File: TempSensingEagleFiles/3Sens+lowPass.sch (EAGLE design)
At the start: 21 parts, among them U1 MLX90614_, U2 MLX90614_, U3 MLX90614_

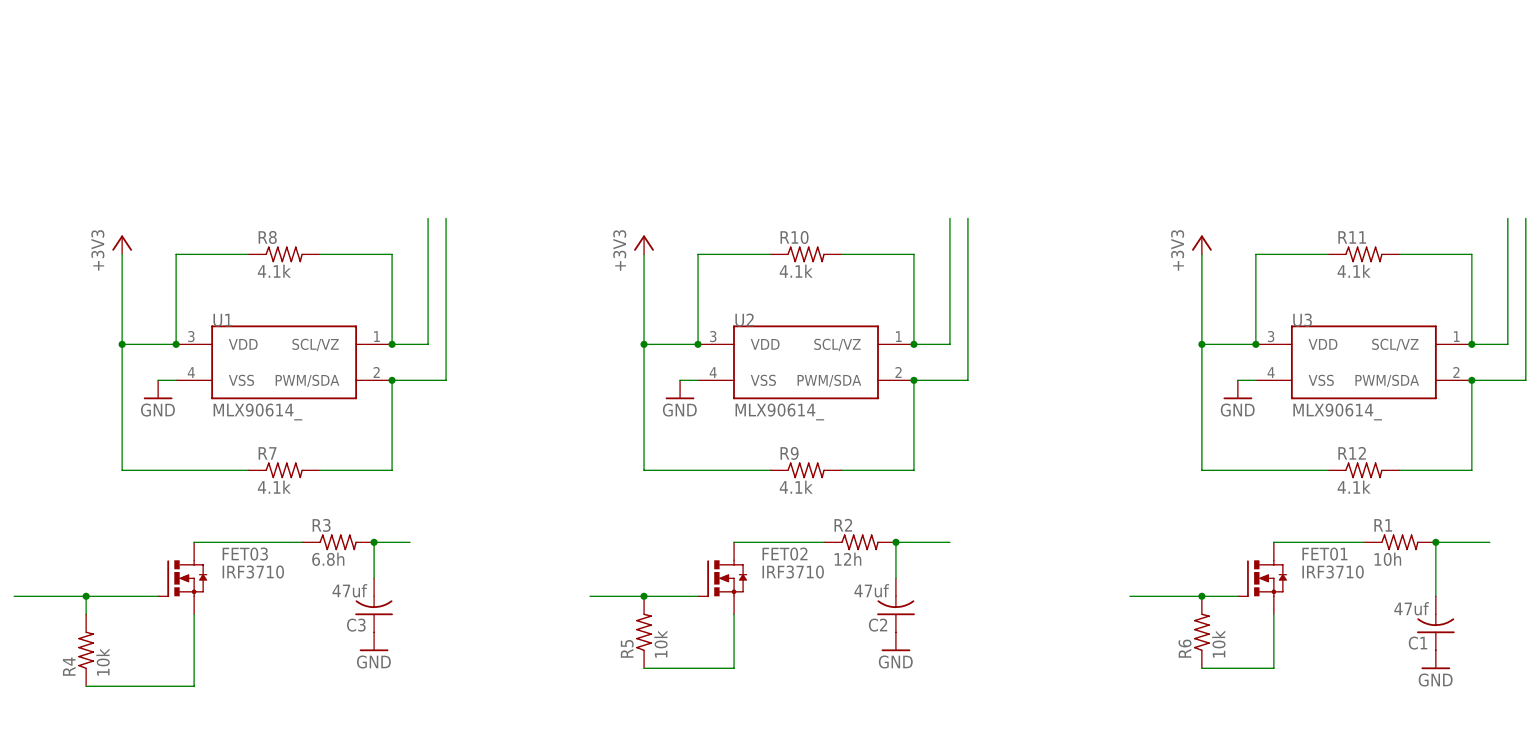
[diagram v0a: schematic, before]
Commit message: worked on Eagle Files
Added 1 Sensor and Main board
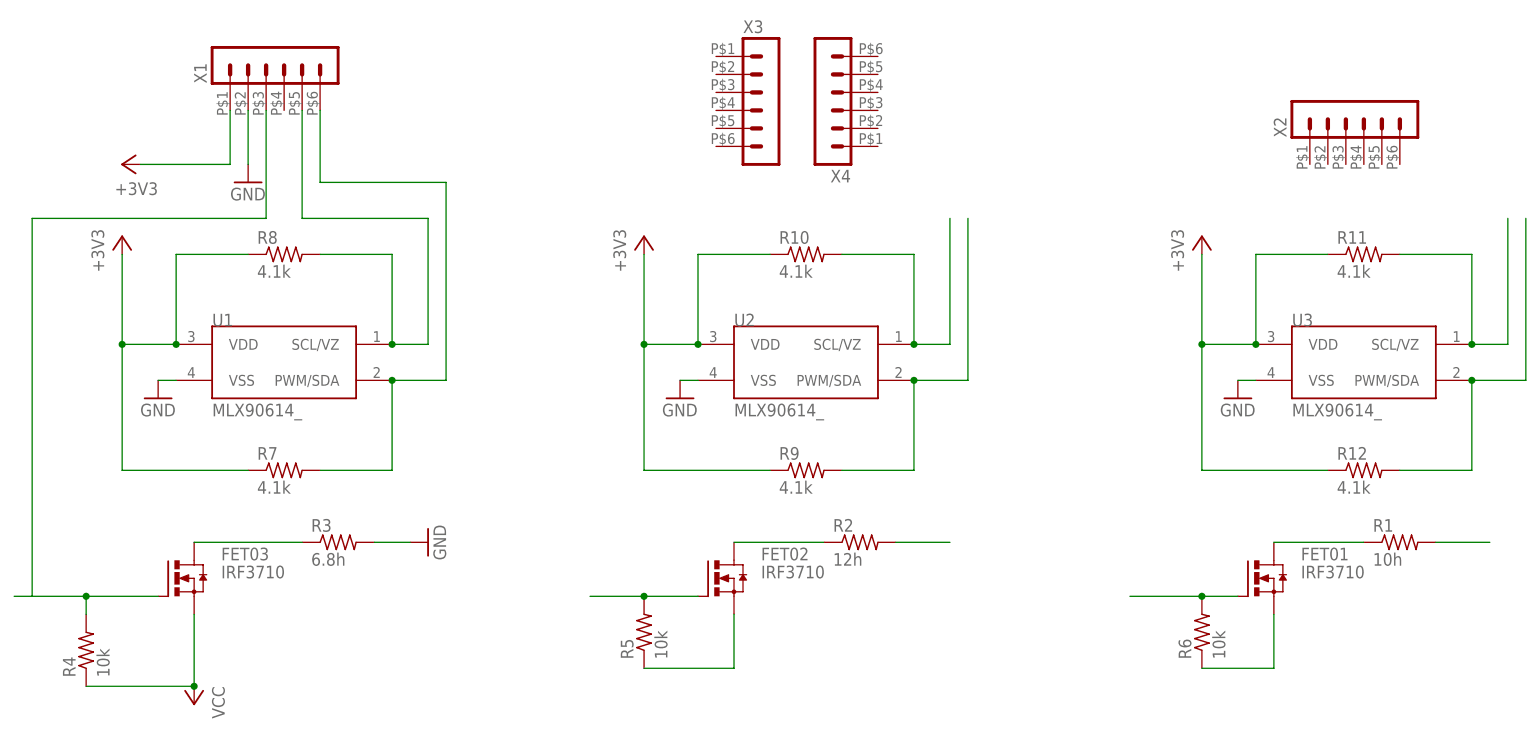
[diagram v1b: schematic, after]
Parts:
- removed C1, C2, C3: 47uf, rcl:C-US025-024X044
- added X1, X2: (no value), con-molex-micro-fit-3_0:HEADER_POS6_43045-0600
- added X3, X4: (no value), con-molex-micro-fit-3_0:HEADER_POS6_43650-0600
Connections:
- net N$2 renamed VCC
- removed net N$7: C3.2, R3.2
- net +3V3: now also X1.1
- net GND: now also R3.2, X1.2; no longer C1.1, C2.1, C3.1
- net N$1: now also X1.5
- net N$10: no longer C2.2
- net N$11: no longer C1.2
- net N$8: now also X1.6
- net N$9: now also X1.3
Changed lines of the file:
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@@
 <?xml version="1.0" encoding="utf-8"?>
 <!DOCTYPE eagle SYSTEM "eagle.dtd">
-<eagle version="6.4">
+<eagle version="6.6.0">
 <drawing>
 <settings>
@@
 <part name="FET02" library="transistor-power" deviceset="IRF3704" device="" value="IRF3710"/>
 <part name="FET03" library="transistor-power" deviceset="IRF3704" device="" value="IRF3710"/>
-<part name="C1" library="rcl" deviceset="C-US" device="025-024X044" value="47uf"/>
-<part name="C2" library="rcl" deviceset="C-US" device="025-024X044" value="47uf"/>
-<part name="C3" library="rcl" deviceset="C-US" device="025-024X044" value="47uf"/>
 <part name="R1" library="resistor" deviceset="R-US_" device="0204/2V" value="10h"/>
 <part name="R2" library="resistor" deviceset="R-US_" device="0204/2V" value="12h"/>
@@
 <part name="+3V2" library="supply1" deviceset="+3V3" device=""/>
 <part name="+3V3" library="supply1" deviceset="+3V3" device=""/>
-<part name="GND1" library="supply1" deviceset="GND" device=""/>
+<part name="GNDLEFT" library="supply1" deviceset="GND" device=""/>
 <part name="GND2" library="supply1" deviceset="GND" device=""/>
 <part name="GND3" library="supply1" deviceset="GND" device=""/>
-<part name="+3V1" library="supply1" deviceset="+3V3" device=""/>
-<part name="GND4" library="supply1" deviceset="GND" device=""/>
-<part name="GND5" library="supply1" deviceset="GND" device=""/>
-<part name="GND6" library="supply1" deviceset="GND" device=""/>
+<part name="+3VLEFT" library="supply1" deviceset="+3V3" device=""/>
+<part name="X1" library="con-molex-micro-fit-3_0" deviceset="HEADER_POS6_?" device="43045-0600"/>
+<part name="X2" library="con-molex-micro-fit-3_0" deviceset="HEADER_POS6_?" device="43045-0600"/>
+<part name="X3" library="con-molex-micro-fit-3_0" deviceset="HEADER_POS6_?" device="43650-0600"/>
+<part name="X4" library="con-molex-micro-fit-3_0" deviceset="HEADER_POS6_?" device="43650-0600"/>
+<part name="+3VLEFT1" library="supply1" deviceset="+3V3" device=""/>
+<part name="GNDLEFT1" library="supply1" deviceset="GND" device=""/>
+<part name="GNDLEFT2" library="supply1" deviceset="GND" device=""/>
+<part name="9VLEFT" library="supply1" deviceset="VCC" device=""/>
 </parts>
 <sheets>
@@
 <instance part="FET02" gate="G$1" x="63.5" y="76.2"/>
 <instance part="FET03" gate="G$1" x="-12.7" y="76.2"/>
-<instance part="C1" gate="G$1" x="165.1" y="68.58" rot="R180"/>
-<instance part="C2" gate="G$1" x="88.9" y="71.12" rot="R180"/>
-<instance part="C3" gate="G$1" x="15.24" y="71.12" rot="R180"/>
 <instance part="R1" gate="G$1" x="160.02" y="81.28"/>
 <instance part="R2" gate="G$1" x="83.82" y="81.28"/>
@@
 <instance part="+3V2" gate="G$1" x="53.34" y="124.46"/>
 <instance part="+3V3" gate="G$1" x="132.08" y="124.46"/>
-<instance part="GND1" gate="1" x="-15.24" y="101.6"/>
+<instance part="GNDLEFT" gate="1" x="-15.24" y="101.6"/>
 <instance part="GND2" gate="1" x="58.42" y="101.6"/>
 <instance part="GND3" gate="1" x="137.16" y="101.6"/>
-<instance part="+3V1" gate="G$1" x="-20.32" y="124.46"/>
-<instance part="GND4" gate="1" x="15.24" y="66.04"/>
-<instance part="GND5" gate="1" x="88.9" y="66.04"/>
-<instance part="GND6" gate="1" x="165.1" y="63.5"/>
+<instance part="+3VLEFT" gate="G$1" x="-20.32" y="124.46"/>
+<instance part="X1" gate="G$1" x="2.54" y="147.32" rot="R90"/>
+<instance part="X2" gate="G$1" x="154.94" y="139.7" rot="R90"/>
+<instance part="X3" gate="G$1" x="68.58" y="142.24"/>
+<instance part="X4" gate="G$1" x="81.28" y="144.78" rot="R180"/>
+<instance part="+3VLEFT1" gate="G$1" x="-20.32" y="134.62" rot="R90"/>
+<instance part="GNDLEFT1" gate="1" x="-2.54" y="132.08"/>
+<instance part="GNDLEFT2" gate="1" x="22.86" y="81.28" rot="R90"/>
+<instance part="9VLEFT" gate="VCC" x="-10.16" y="58.42" rot="R180"/>
 </instances>
 <busses>
 </busses>
 <nets>
-<net name="N$2" class="0">
-<segment>
-<pinref part="R4" gate="G$1" pin="1"/>
-<wire x1="-25.4" y1="60.96" x2="-10.16" y2="60.96" width="0.1524" layer="91"/>
-<pinref part="FET03" gate="G$1" pin="S"/>
-<wire x1="-10.16" y1="60.96" x2="-10.16" y2="71.12" width="0.1524" layer="91"/>
-</segment>
-</net>
 <net name="N$3" class="0">
 <segment>
@@
 <wire x1="-15.24" y1="73.66" x2="-25.4" y2="73.66" width="0.1524" layer="91"/>
 <wire x1="-25.4" y1="73.66" x2="-25.4" y2="71.12" width="0.1524" layer="91"/>
-<wire x1="-25.4" y1="73.66" x2="-35.56" y2="73.66" width="0.1524" layer="91"/>
+<wire x1="-25.4" y1="73.66" x2="-33.02" y2="73.66" width="0.1524" layer="91"/>
 <junction x="-25.4" y="73.66"/>
+<wire x1="-35.56" y1="73.66" x2="-33.02" y2="73.66" width="0.1524" layer="91"/>
+<wire x1="-33.02" y1="73.66" x2="-33.02" y2="127" width="0.1524" layer="91"/>
+<wire x1="-33.02" y1="127" x2="0" y2="127" width="0.1524" layer="91"/>
+<pinref part="X1" gate="G$1" pin="3"/>
+<wire x1="0" y1="127" x2="0" y2="142.24" width="0.1524" layer="91"/>
 </segment>
 </net>
@@
 <wire x1="22.86" y1="109.22" x2="22.86" y2="127" width="0.1524" layer="91"/>
 <junction x="17.78" y="109.22"/>
+<pinref part="X1" gate="G$1" pin="5"/>
+<wire x1="22.86" y1="127" x2="5.08" y2="127" width="0.1524" layer="91"/>
+<wire x1="5.08" y1="127" x2="5.08" y2="142.24" width="0.1524" layer="91"/>
 </segment>
 </net>
@@
 <wire x1="17.78" y1="91.44" x2="7.62" y2="91.44" width="0.1524" layer="91"/>
 <wire x1="17.78" y1="104.14" x2="25.4" y2="104.14" width="0.1524" layer="91"/>
-<wire x1="25.4" y1="104.14" x2="25.4" y2="127" width="0.1524" layer="91"/>
+<wire x1="25.4" y1="104.14" x2="25.4" y2="132.08" width="0.1524" layer="91"/>
 <junction x="17.78" y="104.14"/>
+<pinref part="X1" gate="G$1" pin="6"/>
+<wire x1="25.4" y1="132.08" x2="7.62" y2="132.08" width="0.1524" layer="91"/>
+<wire x1="7.62" y1="132.08" x2="7.62" y2="142.24" width="0.1524" layer="91"/>
 </segment>
 </net>
@@
 <segment>
 <pinref part="U1" gate="G$1" pin="VSS"/>
-<pinref part="GND1" gate="1" pin="GND"/>
+<pinref part="GNDLEFT" gate="1" pin="GND"/>
 <wire x1="-15.24" y1="104.14" x2="-12.7" y2="104.14" width="0.1524" layer="91"/>
 </segment>
@@
 </segment>
 <segment>
-<pinref part="C3" gate="G$1" pin="1"/>
-<pinref part="GND4" gate="1" pin="GND"/>
-</segment>
-<segment>
-<pinref part="C2" gate="G$1" pin="1"/>
-<pinref part="GND5" gate="1" pin="GND"/>
-</segment>
-<segment>
-<pinref part="C1" gate="G$1" pin="1"/>
-<pinref part="GND6" gate="1" pin="GND"/>
+<pinref part="X1" gate="G$1" pin="2"/>
+<pinref part="GNDLEFT1" gate="1" pin="GND"/>
+<wire x1="-2.54" y1="142.24" x2="-2.54" y2="134.62" width="0.1524" layer="91"/>
+</segment>
+<segment>
+<pinref part="R3" gate="G$1" pin="2"/>
+<wire x1="15.24" y1="81.28" x2="20.32" y2="81.28" width="0.1524" layer="91"/>
+<pinref part="GNDLEFT2" gate="1" pin="GND"/>
 </segment>
 </net>
@@
 <wire x1="-20.32" y1="91.44" x2="-20.32" y2="109.22" width="0.1524" layer="91"/>
 <wire x1="-20.32" y1="109.22" x2="-20.32" y2="121.92" width="0.1524" layer="91"/>
-<pinref part="+3V1" gate="G$1" pin="+3V3"/>
+<pinref part="+3VLEFT" gate="G$1" pin="+3V3"/>
 <junction x="-12.7" y="109.22"/>
 <junction x="-20.32" y="109.22"/>
@@
 <junction x="132.08" y="109.22"/>
 </segment>
-</net>
-<net name="N$7" class="0">
-<segment>
-<pinref part="C3" gate="G$1" pin="2"/>
-<pinref part="R3" gate="G$1" pin="2"/>
-<wire x1="15.24" y1="76.2" x2="15.24" y2="81.28" width="0.1524" layer="91"/>
-<wire x1="15.24" y1="81.28" x2="20.32" y2="81.28" width="0.1524" layer="91"/>
-<junction x="15.24" y="81.28"/>
+<segment>
+<pinref part="+3VLEFT1" gate="G$1" pin="+3V3"/>
+<pinref part="X1" gate="G$1" pin="1"/>
+<wire x1="-17.78" y1="134.62" x2="-5.08" y2="134.62" width="0.1524" layer="91"/>
+<wire x1="-5.08" y1="134.62" x2="-5.08" y2="142.24" width="0.1524" layer="91"/>
 </segment>
 </net>
 <net name="N$10" class="0">
 <segment>
-<pinref part="C2" gate="G$1" pin="2"/>
 <pinref part="R2" gate="G$1" pin="2"/>
-<wire x1="88.9" y1="76.2" x2="88.9" y2="81.28" width="0.1524" layer="91"/>
 <wire x1="88.9" y1="81.28" x2="96.52" y2="81.28" width="0.1524" layer="91"/>
-<junction x="88.9" y="81.28"/>
 </segment>
 </net>
 <net name="N$11" class="0">
 <segment>
-<pinref part="C1" gate="G$1" pin="2"/>
 <pinref part="R1" gate="G$1" pin="2"/>
-<wire x1="165.1" y1="73.66" x2="165.1" y2="81.28" width="0.1524" layer="91"/>
 <wire x1="165.1" y1="81.28" x2="172.72" y2="81.28" width="0.1524" layer="91"/>
-<junction x="165.1" y="81.28"/>
 </segment>
 </net>
@@
 </segment>
 </net>
+<net name="VCC" class="0">
+<segment>
+<pinref part="R4" gate="G$1" pin="1"/>
+<wire x1="-25.4" y1="60.96" x2="-10.16" y2="60.96" width="0.1524" layer="91"/>
+<pinref part="FET03" gate="G$1" pin="S"/>
+<wire x1="-10.16" y1="60.96" x2="-10.16" y2="71.12" width="0.1524" layer="91"/>
+<pinref part="9VLEFT" gate="VCC" pin="VCC"/>
+<junction x="-10.16" y="60.96"/>
+</segment>
+</net>
